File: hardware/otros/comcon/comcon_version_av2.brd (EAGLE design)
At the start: 91.7 x 73.3 mm, 148 parts, among them IC1 74LS32N, IC10 74LS365N, IC11 74LS365N, IC12 74LS365N, IC13 74LS365N, IC14 74LS365N, IC2 74LS366N, IC7 74LS365N, IC8 74LS365N, IC9 74LS365N

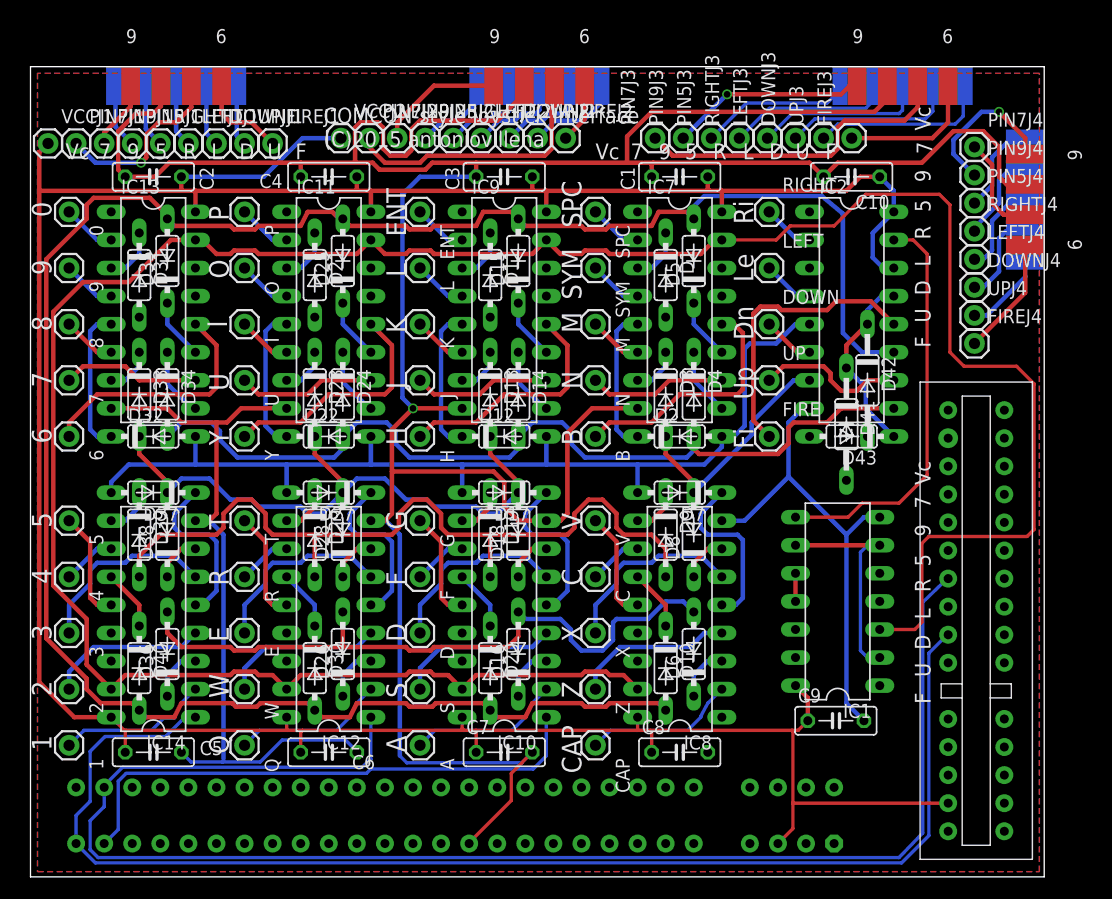
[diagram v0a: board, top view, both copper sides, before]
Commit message: 
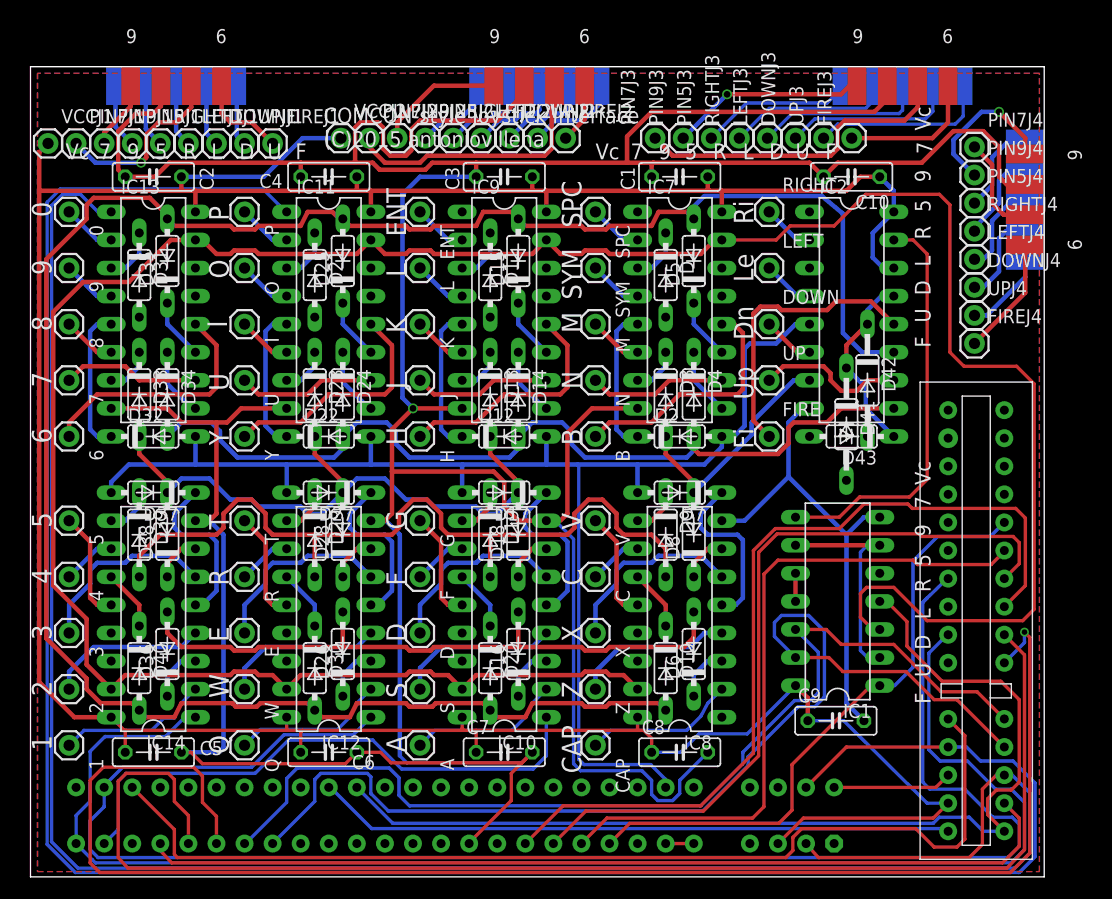
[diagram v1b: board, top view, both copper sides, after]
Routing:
- net A13: track 0.00 -> 202.4 mm
- net A12: track 0.00 -> 187.0 mm
- net A5: track 0.00 -> 134.9 mm, vias 0 -> 1
- net A4: track 0.00 -> 122.2 mm
- net A7: track 0.00 -> 98.3 mm
- net A8: track 0.00 -> 93.6 mm
- net /RD: track 0.00 -> 92.8 mm
- net A6: track 0.00 -> 92.0 mm
- net /ROMCS: track 0.00 -> 83.9 mm
- net A3: track 0.00 -> 78.0 mm
- net A2: track 0.00 -> 68.7 mm
- net A1: track 0.00 -> 61.9 mm
- net GND: track 393.2 -> 453.2 mm
- net /WR: track 0.00 -> 57.7 mm
- net A0: track 0.00 -> 55.8 mm
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
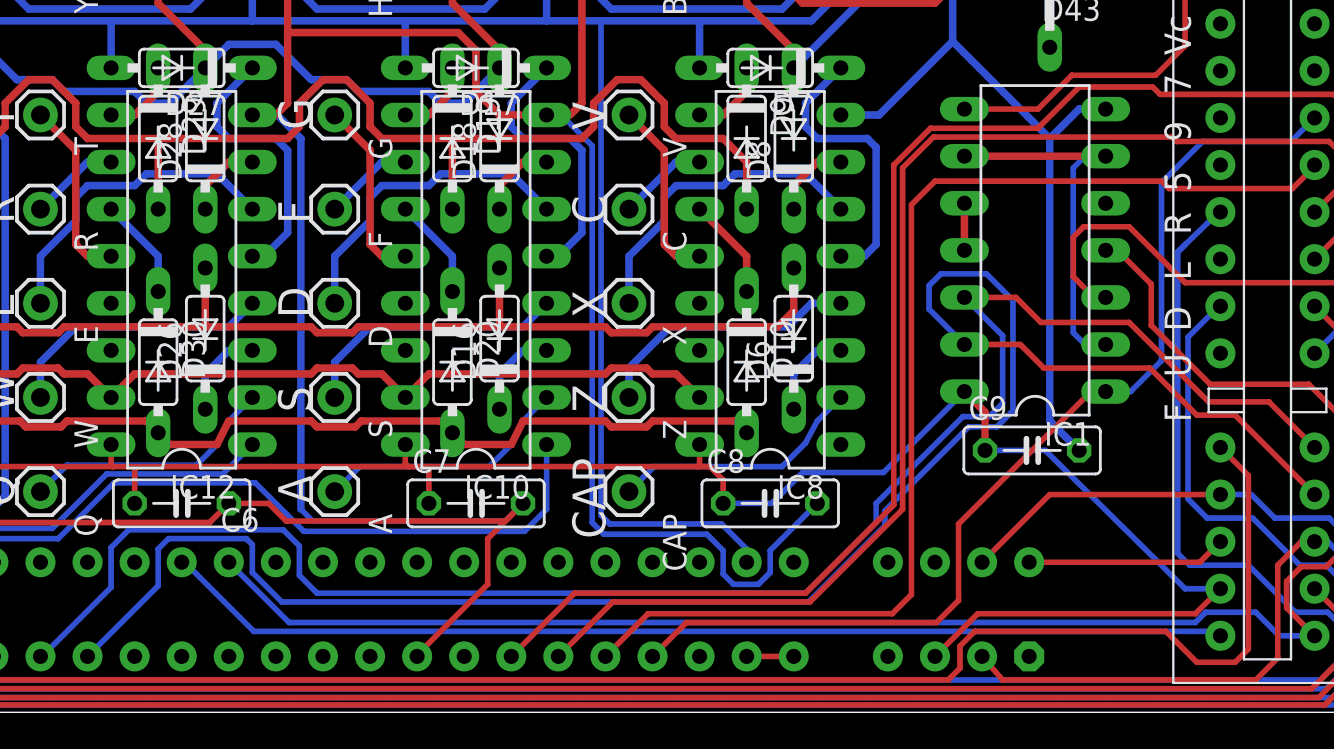
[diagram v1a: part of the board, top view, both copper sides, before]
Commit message: 
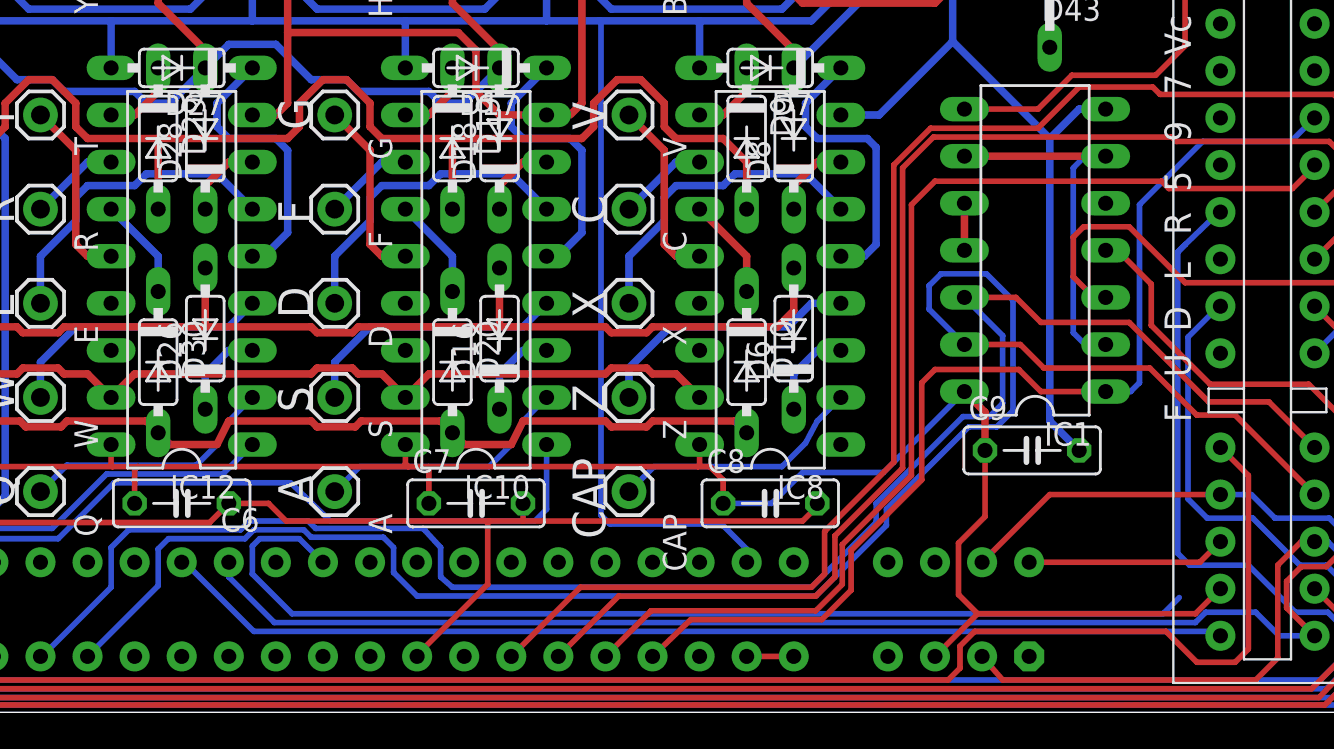
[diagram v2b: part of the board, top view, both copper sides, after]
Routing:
- net GND: track 453.2 -> 392.3 mm
- net /MREQ: track 0.00 -> 57.3 mm
- net VCC: track 285.6 -> 279.6 mm
- net A0: track 55.8 -> 58.7 mm
- net A1: track 61.9 -> 59.4 mm

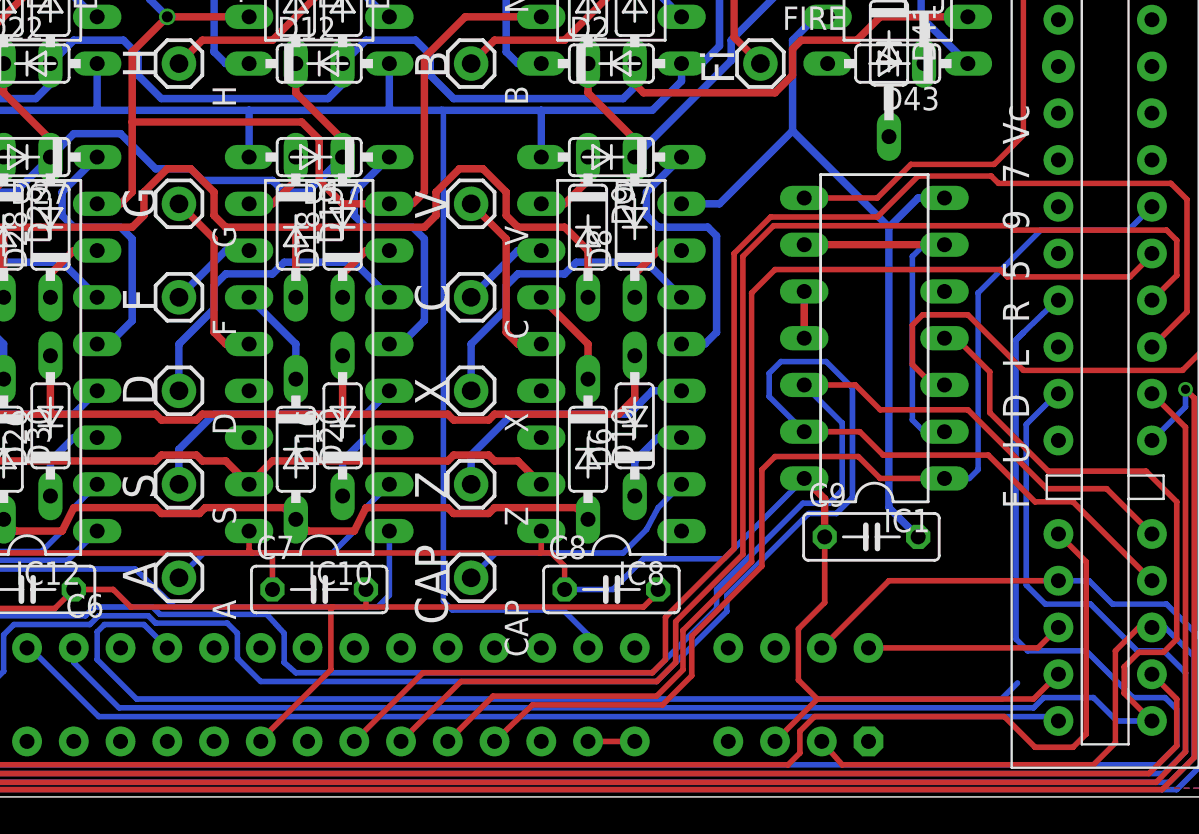
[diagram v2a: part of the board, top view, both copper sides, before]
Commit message: 
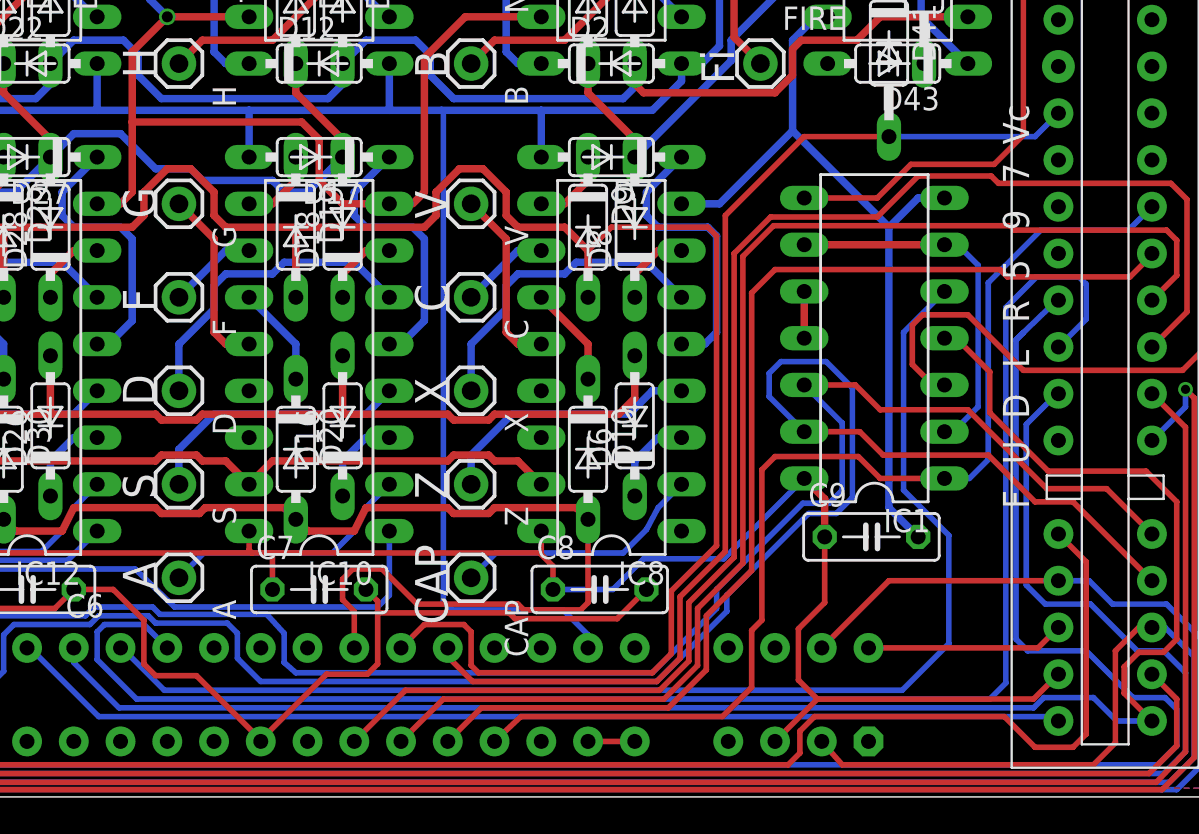
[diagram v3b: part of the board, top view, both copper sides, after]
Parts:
- moved C8 0.63 mm to (58.1, 11.3)
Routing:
- net /IORQ: track 0.00 -> 68.1 mm
- net D5: track 0.00 -> 59.7 mm
- net D3: track 154.6 -> 203.9 mm
- net /MREQ: track 57.3 -> 86.3 mm
- net D4: track 197.5 -> 220.6 mm
- net A0: track 58.7 -> 60.9 mm
- net A3: track 78.0 -> 78.8 mm
- net A2: track 68.7 -> 69.5 mm
- net A1: track 59.4 -> 60.2 mm
- net /RDIO: track 20.5 -> 20.0 mm

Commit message: 
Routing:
- net D6: track 0.00 -> 60.1 mm
- net D2: track 76.9 -> 129.0 mm
- net D7: track 0.00 -> 52.0 mm
- net A14: track 0.00 -> 46.3 mm, vias 0 -> 1
- net A8: track 93.6 -> 135.6 mm, vias 0 -> 1
- net D5: track 59.7 -> 49.9 mm
- net GND: track 392.6 -> 398.6 mm
- net D3: track 203.9 -> 199.4 mm
- net A7: track 98.4 -> 99.2 mm

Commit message: 
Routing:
- net A9: track 51.0 -> 146.0 mm, vias 0 -> 1
- net D2: track 129.0 -> 193.5 mm
- net D5: track 49.9 -> 106.8 mm
- net D0: track 59.9 -> 109.0 mm
- net D4: track 220.6 -> 248.8 mm
- net D1: track 126.0 -> 149.3 mm
- net GND: track 398.6 -> 415.4 mm
- net D3: track 199.4 -> 204.4 mm
- net N$69: track 15.2 -> 13.0 mm

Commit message: 
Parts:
- moved C10 0.56 mm to (74.3, 63.9)
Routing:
- net D0: track 109.0 -> 176.3 mm
- net A5: track 134.9 -> 195.0 mm
- net GND: track 415.4 -> 446.2 mm
- net D3: track 204.4 -> 218.2 mm
- net N$78: track 21.7 -> 23.2 mm
- net N$22: track 22.4 -> 23.2 mm
- net VCC: track 279.6 -> 280.3 mm
- net D2: track 193.5 -> 192.8 mm
